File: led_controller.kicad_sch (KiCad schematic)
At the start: 56 parts

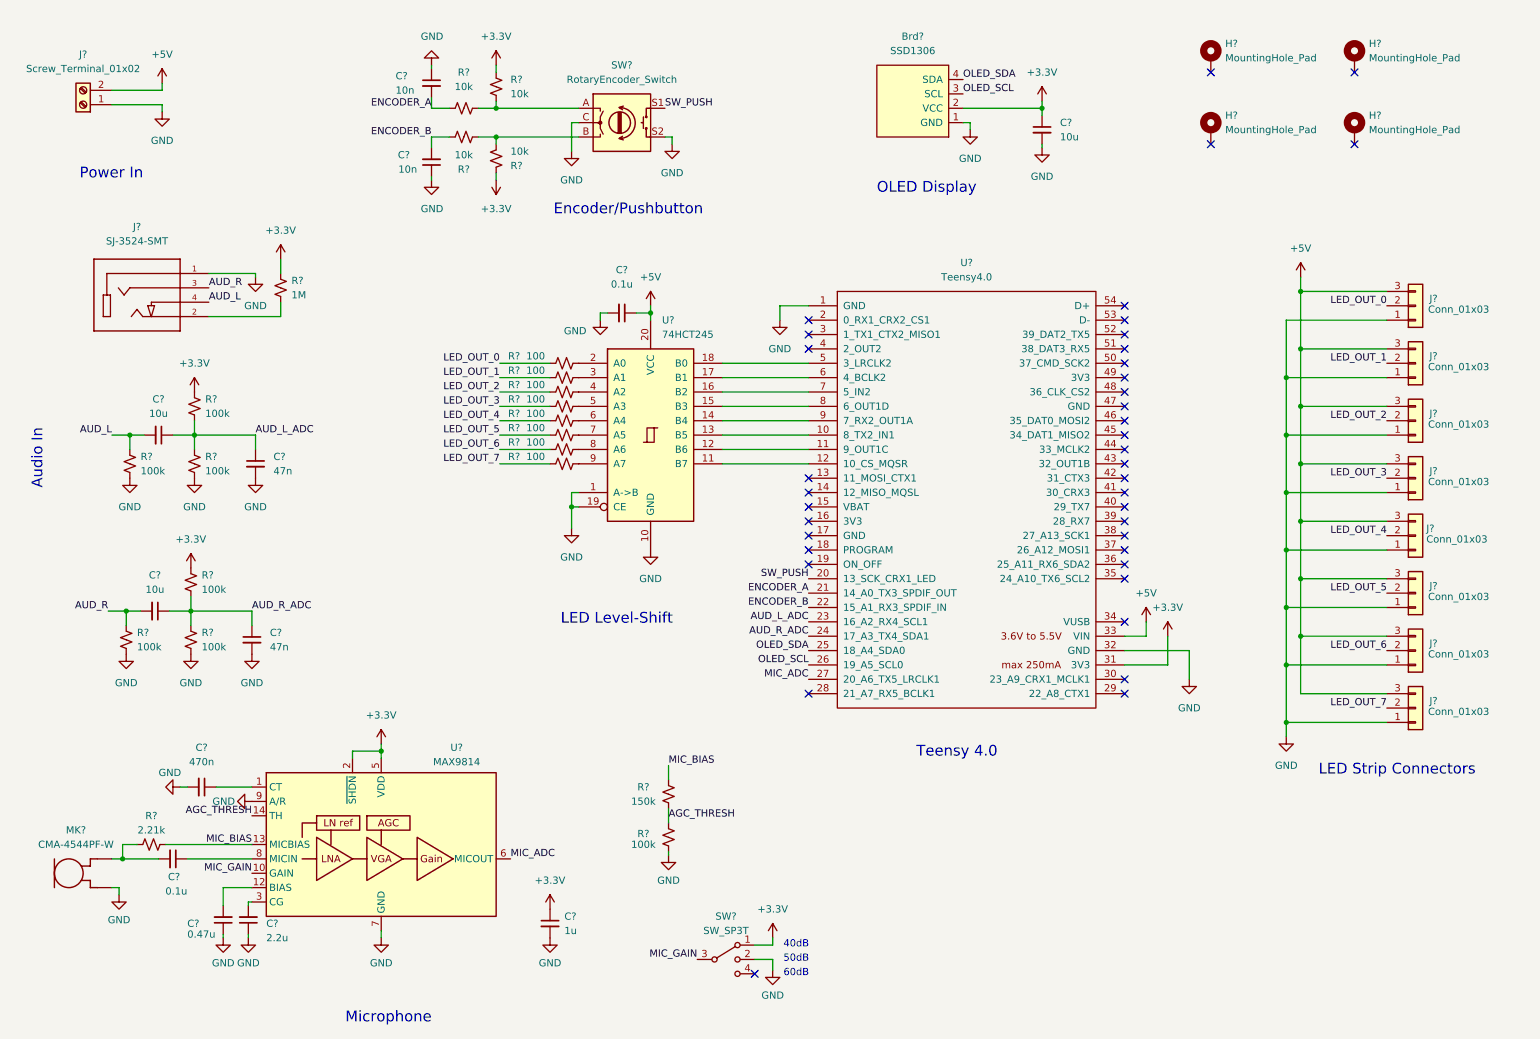
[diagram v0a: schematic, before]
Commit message: Start layout, choose display
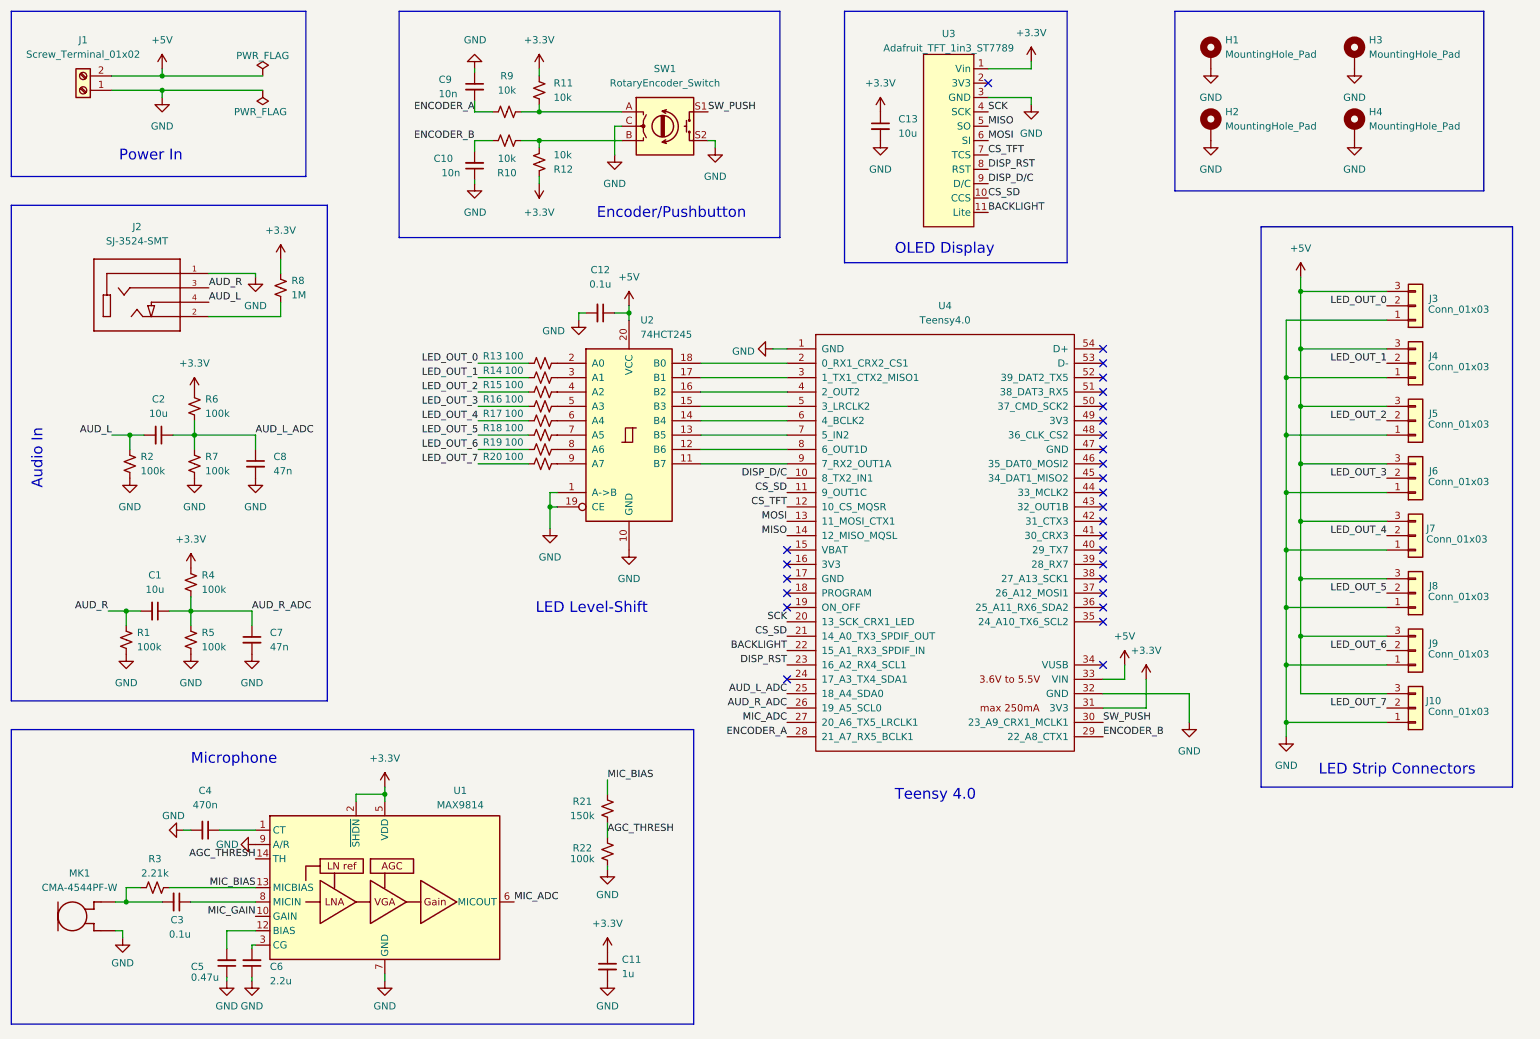
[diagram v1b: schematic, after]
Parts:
- removed Brd?: SSD1306, symbol SSD1306-128x64_OLED:SSD1306
- removed SW?: SW_SP3T, symbol Switch:SW_SP3T
- added U3: Adafruit_TFT_1in3_ST7789, displays:Adafruit_TFT_1in3_ST7789, symbol displays:Adafruit_TFT_1in3_ST7789
- C1, C10, C11, C12, C13, C2, C3, C4, C5, C6, C7, C8, C9: renamed from C?; footprint (none) -> Capacitor_SMD:C_0805_2012Metric_Pad1.18x1.45mm_HandSolder
- H1, H2, H3, H4: renamed from H?; footprint (none) -> MountingHole:MountingHole_3.2mm_M3_ISO14580_Pad
- J1: renamed from J?; footprint (none) -> terminal_block:TerminalBlock_Molex_393570002_1x02_P3.50mm_Horizontal
- J10, J3, J4, J5, J6, J7, J8, J9: renamed from J?; footprint (none) -> Connector_JST:JST_PH_S3B-PH-K_1x03_P2.00mm_Horizontal
- J2: renamed from J?; footprint CUI_SJ-3524-SMT -> SJ-3524-SMT:CUI_SJ-3524-SMT
- MK1: renamed from MK?; footprint (none) -> CMA-4544PF-W:MIC_CMA-4544PF-W
- R1, R10, R11, R12, R13, R14, R15, R16, R17, R18, R19, R2, R20, R21, R22, R3, R4, R5, R6, R7, R8, R9: renamed from R?; footprint (none) -> Resistor_SMD:R_0805_2012Metric_Pad1.20x1.40mm_HandSolder
- SW1: renamed from SW?; footprint (none) -> Rotary_Encoder:RotaryEncoder_Alps_EC11E-Switch_Vertical_H20mm
- U1: renamed from U?; footprint (none) -> Package_DFN_QFN:TDFN-14-1EP_3x3mm_P0.4mm_EP1.78x2.35mm_ThermalVias
- U2: renamed from U?; footprint (none) -> Package_SO:TSSOP-20_4.4x6.5mm_P0.65mm
- U4: renamed from U?; footprint (none) -> teensy_library:Teensy40
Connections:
- net OLED_SCL is gone; now on net AUD_R_ADC: U4.26 (19_A5_SCL0)
- net OLED_SDA is gone; now on net AUD_L_ADC: U4.25 (18_A4_SDA0)
- net +3V3: now also U3.1 (Vin)
- net AUD_L_ADC: no longer U4.23 (16_A2_RX4_SCL1)
- net AUD_R_ADC: no longer U4.24 (17_A3_TX4_SDA1)
- net ENCODER_A: now also U4.28 (21_A7_RX5_BCLK1); no longer U4.21 (14_A0_TX3_SPDIF_OUT)
- net ENCODER_B: now also U4.29 (22_A8_CTX1); no longer U4.22 (15_A1_RX3_SPDIF_IN)
- net GND: now also H1.1, H2.1, H3.1, H4.1, U3.3 (GND)
- net SW_PUSH: now also U4.30 (23_A9_CRX1_MCLK1); no longer U4.20 (13_SCK_CRX1_LED)
- net at U2.11 (B7): now also U4.9 (7_RX2_OUT1A); no longer U4.12 (10_CS_MQSR)
- net at U2.12 (B6): now also U4.8 (6_OUT1D); no longer U4.11 (9_OUT1C)
- net at U2.13 (B5): now also U4.7 (5_IN2); no longer U4.10 (8_TX2_IN1)
- net at U2.14 (B4): now also U4.6 (4_BCLK2); no longer U4.9 (7_RX2_OUT1A)
- net at U2.15 (B3): now also U4.5 (3_LRCLK2); no longer U4.8 (6_OUT1D)
- net at U2.16 (B2): now also U4.4 (2_OUT2); no longer U4.7 (5_IN2)
- net at U2.17 (B1): now also U4.3 (1_TX1_CTX2_MISO1); no longer U4.6 (4_BCLK2)
- net at U2.18 (B0): now also U4.2 (0_RX1_CRX2_CS1); no longer U4.5 (3_LRCLK2)
- net MOSI: now reaches U4.13 (11_MOSI_CTX1)
- net MOSI: now also U3.6 (SI)
- net MISO: now reaches U4.14 (12_MISO_MQSL)
- net MISO: now also U3.5 (SO)
- new net BACKLIGHT: U3.11 (Lite), U4.22 (15_A1_RX3_SPDIF_IN)
- new net CS_SD: U3.10 (CCS), U4.11 (9_OUT1C), U4.21 (14_A0_TX3_SPDIF_OUT)
- new net CS_TFT: U3.7 (TCS), U4.12 (10_CS_MQSR)
- new net DISP_D/C: U3.9 (D/C), U4.10 (8_TX2_IN1)
- new net DISP_RST: U3.8 (RST), U4.23 (16_A2_RX4_SCL1)
- new net SCK: U3.4 (SCK), U4.20 (13_SCK_CRX1_LED)
- no-connect marks 39 -> 28
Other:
- note removed: "40dB"
- note removed: "50dB"
- note removed: "60dB"
- moved on the sheet: C10, C11, C12, C13, C3, C4, C5, C6, C9, H1, H2, H3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

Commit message: Place passives, route all except power
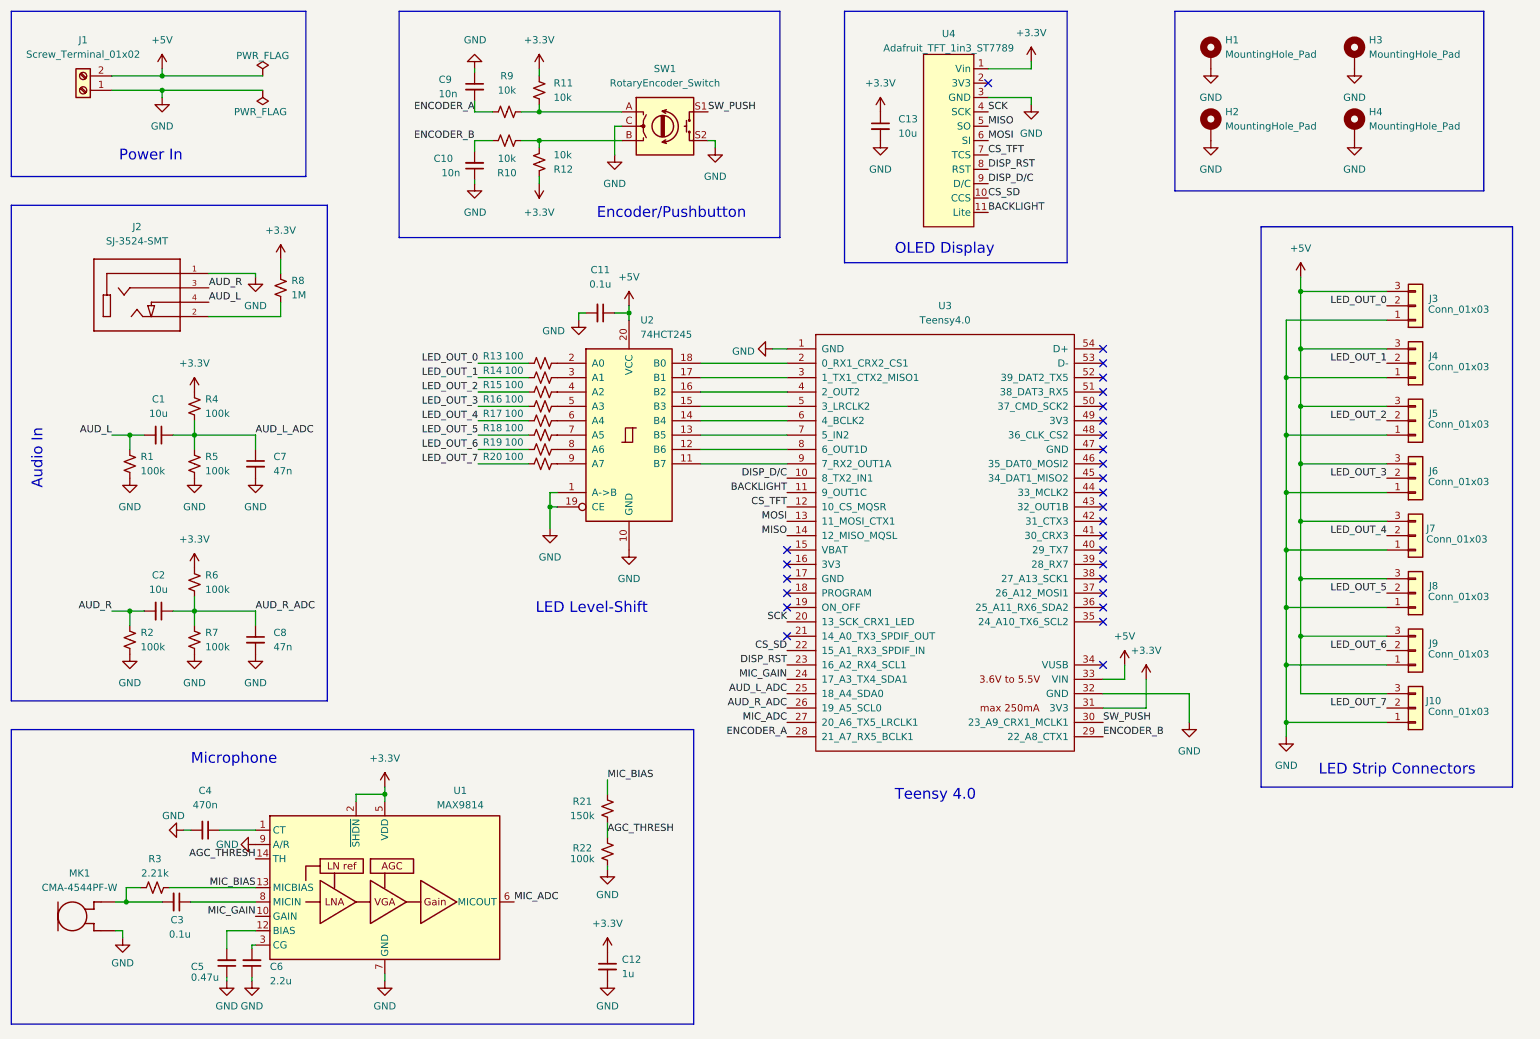
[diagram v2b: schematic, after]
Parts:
- renumbered C2 to C1, C12 to C11, C11 to C12, C1 to C2, C8 to C7, C7 to C8, R2 to R1, R1 to R2, R6 to R4, R7 to R5, R4 to R6, R5 to R7, U4 to U3, U3 to U4
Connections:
- net BACKLIGHT: now also U3.11 (9_OUT1C); no longer U3.22 (15_A1_RX3_SPDIF_IN)
- net CS_SD: now also U3.22 (15_A1_RX3_SPDIF_IN); no longer U3.11 (9_OUT1C), U3.21 (14_A0_TX3_SPDIF_OUT)
- net MIC_GAIN: now also U3.24 (17_A3_TX4_SDA1)
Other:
- moved on the sheet: C2, C8, R2, R6, R7

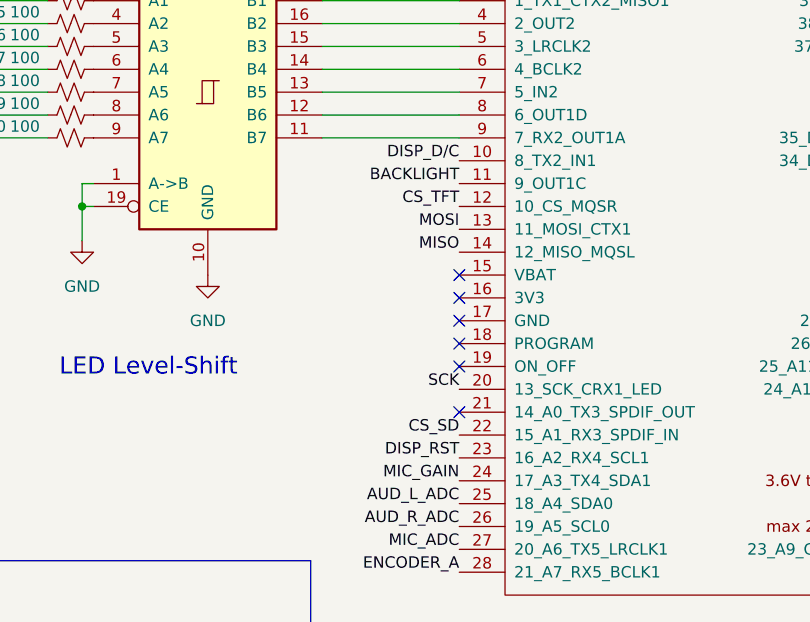
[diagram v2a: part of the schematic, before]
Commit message: Rearrange screen and power, add 3D models
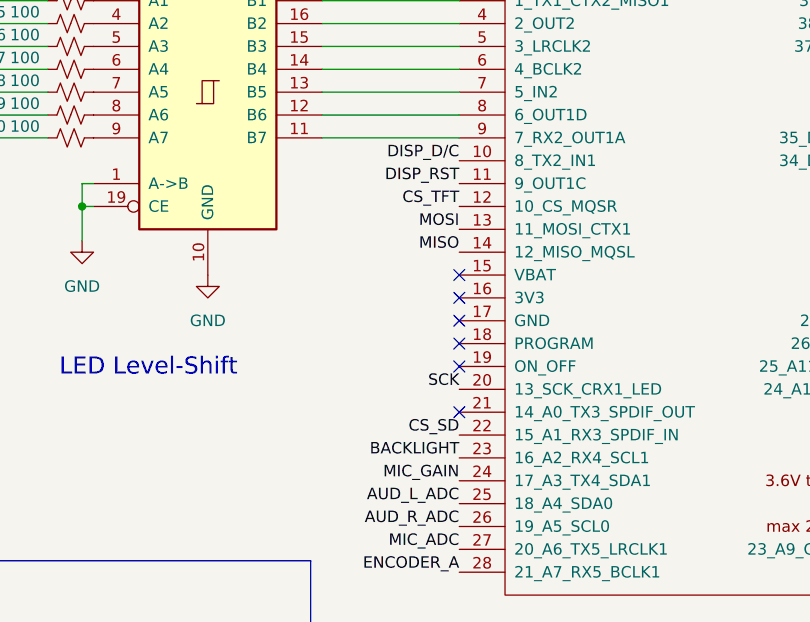
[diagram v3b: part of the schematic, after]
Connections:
- net BACKLIGHT: now also U3.23 (16_A2_RX4_SCL1); no longer U3.11 (9_OUT1C)
- net DISP_RST: now also U3.11 (9_OUT1C); no longer U3.23 (16_A2_RX4_SCL1)
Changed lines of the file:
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@@
     (effects (font (size 1.27 1.27)) (justify right bottom))
   )
-  (label "BACKLIGHT" (at 153.67 99.06 180)
+  (label "BACKLIGHT" (at 153.67 129.54 180)
     (effects (font (size 1.27 1.27)) (justify right bottom))
   )
@@
     (effects (font (size 1.27 1.27)) (justify right bottom))
   )
-  (label "DISP_RST" (at 153.67 129.54 180)
+  (label "DISP_RST" (at 153.67 99.06 180)
     (effects (font (size 1.27 1.27)) (justify right bottom))
   )

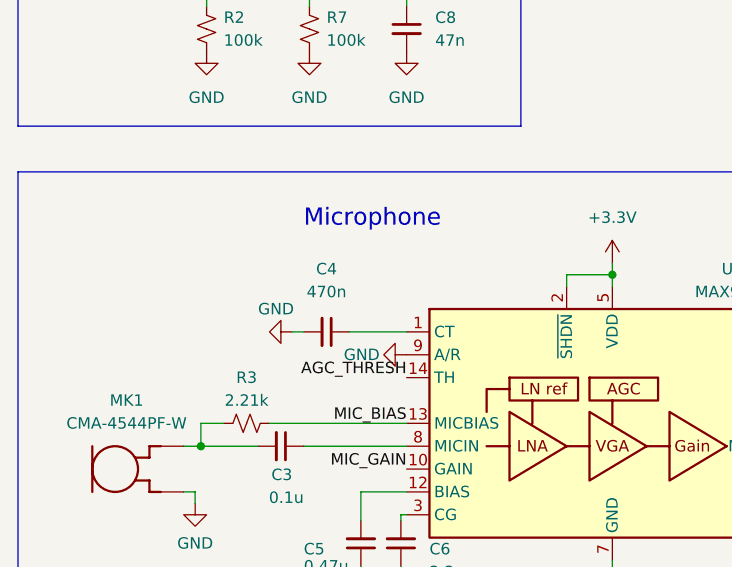
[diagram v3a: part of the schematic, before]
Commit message: Finish routing, add text, via grid, round tracks
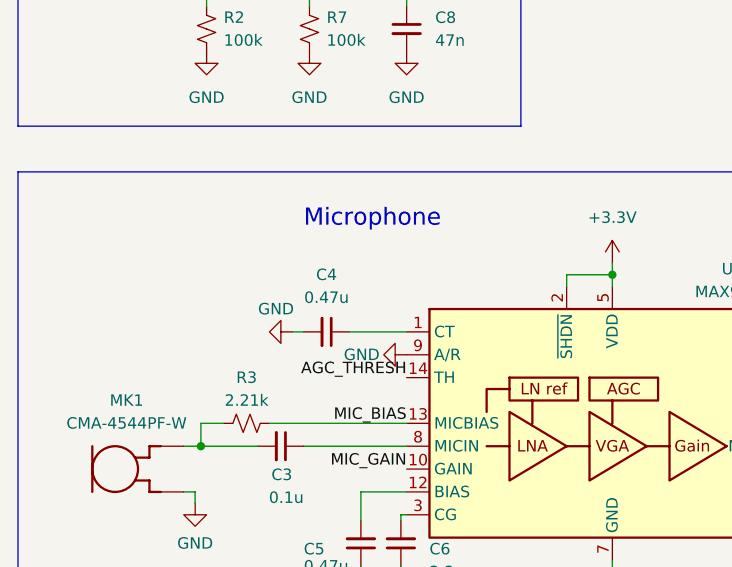
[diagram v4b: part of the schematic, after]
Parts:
- C4: value 470n -> 0.47u
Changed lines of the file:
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@@
   (symbol (lib_id "Device:C_Small") (at 50.8 158.75 270) (unit 1)
     (in_bom yes) (on_board yes) (fields_autoplaced)
-    (property "Reference" "C4" (id 0) (at 50.7936 151.765 90))
-    (property "Value" "470n" (id 1) (at 50.7936 154.305 90))
+    (property "Reference" "C4" (id 0) (at 50.7936 152.4 90))
+    (property "Value" "0.47u" (id 1) (at 50.7936 154.94 90))
     (property "Footprint" "Capacitor_SMD:C_0805_2012Metric_Pad1.18x1.45mm_HandSolder" (id 2) (at 50.8 158.75 0)
       (effects (font (size 1.27 1.27)) hide)
@@
     )
     (path "/5a9cf46d-6415-426d-ad2b-321300b09d80"
-      (reference "C4") (unit 1) (value "470n") (footprint "Capacitor_SMD:C_0805_2012Metric_Pad1.18x1.45mm_HandSolder")
+      (reference "C4") (unit 1) (value "0.47u") (footprint "Capacitor_SMD:C_0805_2012Metric_Pad1.18x1.45mm_HandSolder")
     )
     (path "/8c2fe5b2-2268-4e75-9ea0-430785245297"
